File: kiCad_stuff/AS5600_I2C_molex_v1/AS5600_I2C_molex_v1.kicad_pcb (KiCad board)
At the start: 2 copper layers, 22 x 21.4 mm, 8 parts, among them J1 Conn_01x04, U1 AS5600_ASOM_molex_v1

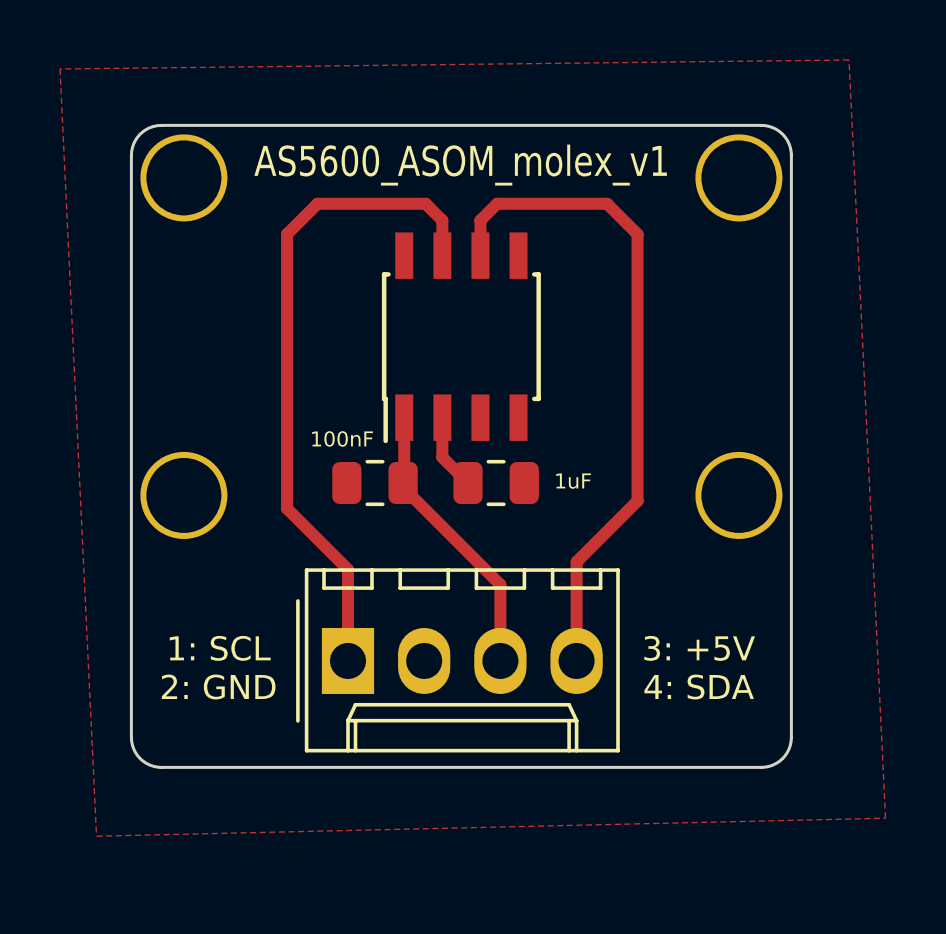
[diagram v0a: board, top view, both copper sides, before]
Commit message: Regenerated ground plane as was overlapping a track
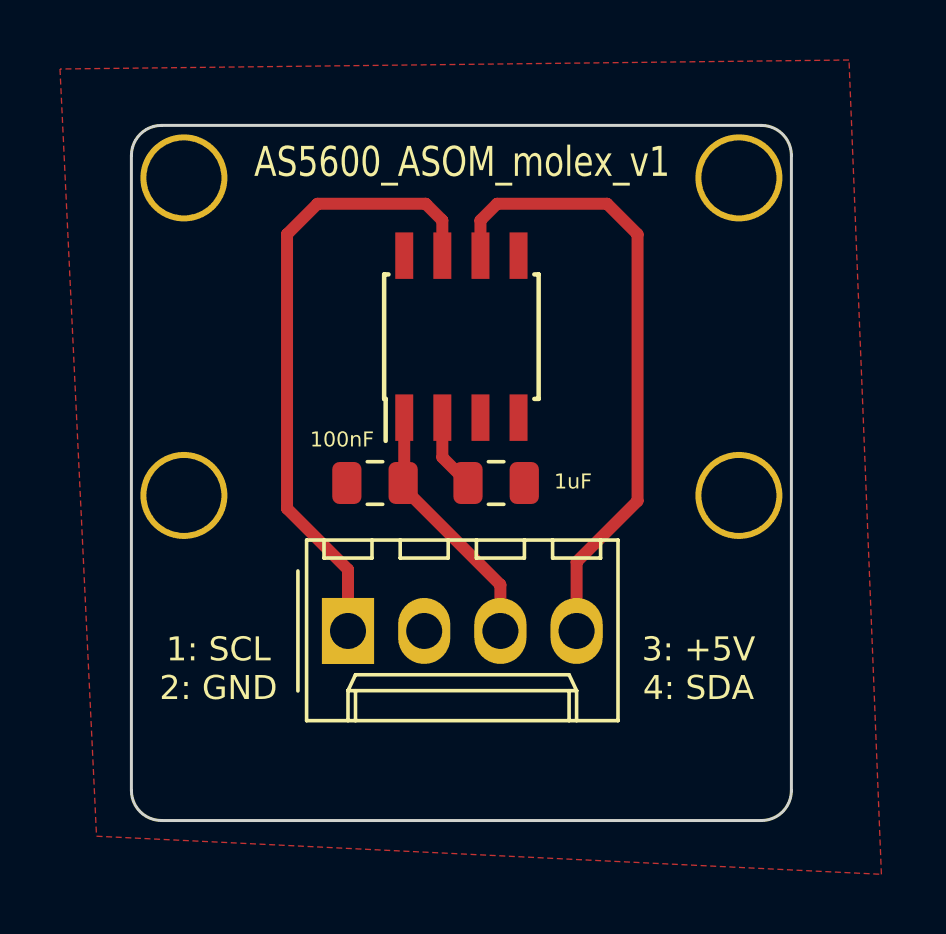
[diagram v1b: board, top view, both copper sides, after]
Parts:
- moved J1 1.00 mm to (164.7, 85.4)
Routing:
- net SDA: track 22.1 -> 21.1 mm
- net SCL: track 22.1 -> 21.1 mm
- net +5V: track 9.53 -> 8.53 mm
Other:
- board size 22 x 21.4 mm -> 22 x 23.2 mm
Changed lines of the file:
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@@
   )
   (module Connector_Molex:Molex_KK-254_AE-6410-04A_1x04_P2.54mm_Vertical (layer F.Cu)
-    (at 164.7 86.432)
+    (at 164.7 85.432)
     (descr "Molex KK-254 Interconnect System, old/engineering part number: AE-6410-04A example for new part number: 22-27-2041, 4 Pins (http://www.molex.com/pdm_docs/sd/022272021_sd.pdf), generated with kicad-footprint-generator")
     (tags "connector Molex KK-254 side entry")
@@
   (gr_arc (start 178.48 69.58) (end 179.48 69.58) (angle -90) (layer Edge.Cuts) (width 0.1))
   (gr_arc (start 158.48 69.58) (end 158.48 68.58) (angle -90) (layer Edge.Cuts) (width 0.1))
-  (gr_arc (start 158.48 88.98) (end 157.48 88.98) (angle -90) (layer Edge.Cuts) (width 0.1))
-  (gr_arc (start 178.48 88.98) (end 178.48 89.98) (angle -90) (layer Edge.Cuts) (width 0.1))
-  (gr_line (start 157.48 69.58) (end 157.48 88.9723) (layer Edge.Cuts) (width 0.1))
-  (gr_line (start 158.48 89.98) (end 178.48 89.98) (layer Edge.Cuts) (width 0.1))
-  (gr_line (start 179.48 88.973094) (end 179.48 69.58) (layer Edge.Cuts) (width 0.1))
+  (gr_arc (start 158.48 90.75) (end 157.48 90.75) (angle -90) (layer Edge.Cuts) (width 0.1))
+  (gr_arc (start 178.48 90.751002) (end 178.48 91.751002) (angle -90) (layer Edge.Cuts) (width 0.1))
+  (gr_line (start 157.48 69.58) (end 157.48 90.750275) (layer Edge.Cuts) (width 0.1))
+  (gr_line (start 158.48 91.751002) (end 178.48 91.751002) (layer Edge.Cuts) (width 0.1))
+  (gr_line (start 179.48 90.751002) (end 179.48 69.58) (layer Edge.Cuts) (width 0.1))
   (gr_line (start 178.48 68.58) (end 158.48 68.58) (layer Edge.Cuts) (width 0.1))
   (segment (start 166.575 80.4625) (end 166.5375 80.5) (width 0.4) (layer F.Cu) (net 1))
@@
   (segment (start 166.575 78.322) (end 166.575 80.4625) (width 0.4) (layer F.Cu) (net 1))
   (segment (start 166.5375 80.6495) (end 166.5375 80.5) (width 0.4) (layer F.Cu) (net 1))
-  (segment (start 169.78 86.432) (end 169.78 83.892) (width 0.4) (layer F.Cu) (net 1))
   (segment (start 169.78 83.892) (end 166.5375 80.6495) (width 0.4) (layer F.Cu) (net 1))
+  (segment (start 169.78 83.892) (end 169.78 85.432) (width 0.4) (layer F.Cu) (net 1))
   (segment (start 168.7 80.5) (end 167.845 79.645) (width 0.4) (layer F.Cu) (net 3))
   (segment (start 167.845 79.645) (end 167.845 78.322) (width 0.4) (layer F.Cu) (net 3))
   (segment (start 169.115 71.747) (end 169.115 72.922) (width 0.4) (layer F.Cu) (net 4))
   (segment (start 172.32 83.13) (end 174.352 81.098) (width 0.4) (layer F.Cu) (net 4))
-  (segment (start 172.32 86.432) (end 172.32 83.13) (width 0.4) (layer F.Cu) (net 4))
   (segment (start 174.352 81.098) (end 174.352 72.208) (width 0.4) (layer F.Cu) (net 4))
   (segment (start 174.352 72.208) (end 173.336 71.192) (width 0.4) (layer F.Cu) (net 4))
   (segment (start 173.336 71.192) (end 169.67 71.192) (width 0.4) (layer F.Cu) (net 4))
   (segment (start 169.67 71.192) (end 169.115 71.747) (width 0.4) (layer F.Cu) (net 4))
+  (segment (start 172.32 83.13) (end 172.32 85.432) (width 0.4) (layer F.Cu) (net 4))
   (segment (start 167.845 71.747) (end 167.845 72.922) (width 0.4) (layer F.Cu) (net 5))
   (segment (start 164.7 83.384) (end 162.668 81.352) (width 0.4) (layer F.Cu) (net 5))
-  (segment (start 164.7 86.432) (end 164.7 83.384) (width 0.4) (layer F.Cu) (net 5))
   (segment (start 162.668 81.352) (end 162.668 72.208) (width 0.4) (layer F.Cu) (net 5))
   (segment (start 162.668 72.208) (end 163.684 71.192) (width 0.4) (layer F.Cu) (net 5))
   (segment (start 163.684 71.192) (end 167.29 71.192) (width 0.4) (layer F.Cu) (net 5))
   (segment (start 167.29 71.192) (end 167.845 71.747) (width 0.4) (layer F.Cu) (net 5))
+  (segment (start 164.7 83.384) (end 164.7 85.432) (width 0.4) (layer F.Cu) (net 5))
   (zone (net 2) (net_name GND) (layer F.Cu) (hatch edge 0.508)
     (connect_pads yes (clearance 0.508))
@@
     (polygon
       (pts
-        (xy 181.4 66.4) (xy 155.1 66.7) (xy 156.318 92.274) (xy 182.618 91.674)
+        (xy 181.4 66.4) (xy 155.1 66.7) (xy 156.318 92.274) (xy 182.48 93.544)
       )
     )
